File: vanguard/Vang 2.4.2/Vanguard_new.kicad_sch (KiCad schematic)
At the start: 84 parts, among them J1 USB_C_Receptacle_USB2.0_16P, J2 Micro_SD_Card_Det1, J3 Conn_02x03_Odd_Even, J4 Conn_01x03, J5 Conn_01x03, J6 Conn_01x03, J7 Conn_01x02_Pin, Q1 BSS138, Q2 BSS138, Q3 BSS138, Q4 BSS138, U1 TXB0104D, U10 AP2112K-3.3, U3 ATSAMD11D14A-M, U4 BMP390L, U5 BD1020HFV-TR, U6 AT25DF641A-SH-T, U7 ATmega4809-A, U9 TPS61092, Y1 Crystal

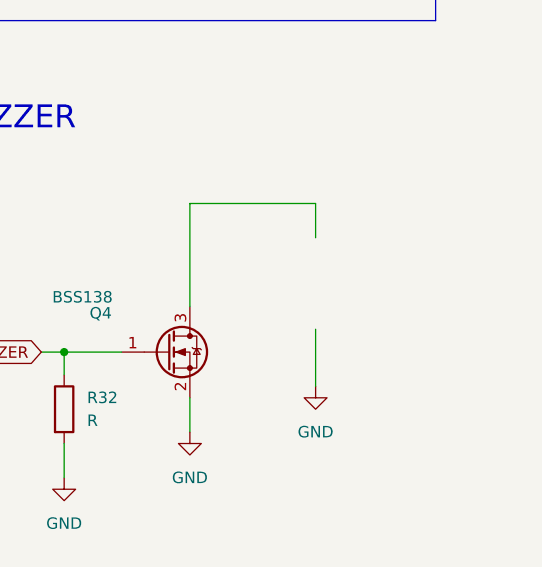
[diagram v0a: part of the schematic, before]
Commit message: added CMI-1295-0585T[1]
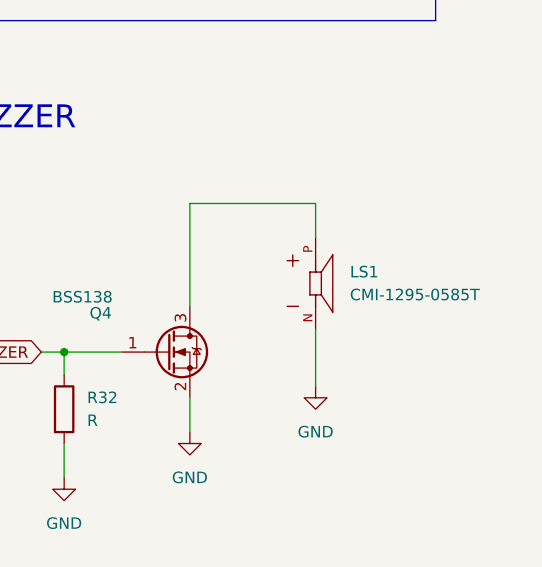
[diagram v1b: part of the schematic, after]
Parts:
- added LS1: CMI-1295-0585T, CMI-1295-0585T:CUI_CMI-1295-0585T, symbol CMI-1295-0585T[1]:CMI-1295-0585T
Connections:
- net GND: now also LS1.N
- net at Q4.3 (D): now also LS1.P
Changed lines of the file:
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@@
+	)
+	(symbol
+		(lib_id "CMI-1295-0585T[1]:CMI-1295-0585T")
+		(at 405.13 106.68 0)
+		(unit 1)
+		(exclude_from_sim no)
+		(in_bom yes)
+		(on_board yes)
+		(dnp no)
+		(fields_autoplaced yes)
+		(property "Reference" "LS1"
+			(at 408.94 105.4099 0)
+			(effects
+				(font
+					(size 1.27 1.27)
+				)
+				(justify left)
+			)
+		)
+		(property "Value" "CMI-1295-0585T"
+			(at 408.94 107.9499 0)
+			(effects
+				(font
+					(size 1.27 1.27)
+				)
+				(justify left)
+			)
+		)
+		(property "Footprint" "CMI-1295-0585T:CUI_CMI-1295-0585T"
+			(at 405.13 106.68 0)
+			(effects
+				(font
+					(size 1.27 1.27)
+				)
+				(justify bottom)
+				(hide yes)
+			)
+		)
+		(property "Datasheet" ""
+			(at 405.13 106.68 0)
+			(effects
+				(font
+					(size 1.27 1.27)
+				)
+				(hide yes)
+			)
+		)
+		(property "Description" ""
+			(at 405.13 106.68 0)
+			(effects
+				(font
+					(size 1.27 1.27)
+				)
+				(hide yes)
+			)
+		)
+		(property "MF" "Same Sky"
+			(at 405.13 106.68 0)
+			(effects
+				(font
+					(size 1.27 1.27)
+				)
+				(justify bottom)
+				(hide yes)
+			)
+		)
+		(property "MAXIMUM_PACKAGE_HEIGHT" "9.7mm"
+			(at 405.13 106.68 0)
+			(effects
+				(font
+					(size 1.27 1.27)
+				)
+				(justify bottom)
+				(hide yes)
+			)
+		)
+		(property "Package" "CUI Inc."
+			(at 405.13 106.68 0)
+			(effects
+				(font
+					(size 1.27 1.27)
+				)
+				(justify bottom)
+				(hide yes)
+			)
+		)
+		(property "Price" "None"
+			(at 405.13 106.68 0)
+			(effects
+				(font
+					(size 1.27 1.27)
+				)
+				(justify bottom)
+				(hide yes)
+			)
+		)
+		(property "Check_prices" "https://www.snapeda.com/parts/CMI-1295-0585T/Same+Sky/view-part/?ref=eda"
+			(at 405.13 106.68 0)
+			(effects
+				(font
+					(size 1.27 1.27)
+				)
+				(justify bottom)
+				(hide yes)
+			)
+		)
+		(property "STANDARD" "Manufacturer Recommendations"
+			(at 405.13 106.68 0)
+			(effects
+				(font
+					(size 1.27 1.27)
+				)
+				(justify bottom)
+				(hide yes)
+			)
+		)
+		(property "PARTREV" "N/A"
+			(at 405.13 106.68 0)
+			(effects
+				(font
+					(size 1.27 1.27)
+				)
+				(justify bottom)
+				(hide yes)
+			)
+		)
+		(property "SnapEDA_Link" "https://www.snapeda.com/parts/CMI-1295-0585T/Same+Sky/view-part/?ref=snap"
+			(at 405.13 106.68 0)
+			(effects
+				(font
+					(size 1.27 1.27)
+				)
+				(justify bottom)
+				(hide yes)
+			)
+		)
+		(property "MP" "CMI-1295-0585T"
+			(at 405.13 106.68 0)
+			(effects
+				(font
+					(size 1.27 1.27)
+				)
+				(justify bottom)
+				(hide yes)
+			)
+		)
+		(property "Description_1" "12 mm, 5 Vdc, 85 dB, Through Hole, Driving Circuit, Magnetic Audio Indicator Buzzer"
+			(at 405.13 106.68 0)
+			(effects
+				(font
+					(size 1.27 1.27)
+				)
+				(justify bottom)
+				(hide yes)
+			)
+		)
+		(property "Availability" "In Stock"
+			(at 405.13 106.68 0)
+			(effects
+				(font
+					(size 1.27 1.27)
+				)
+				(justify bottom)
+				(hide yes)
+			)
+		)
+		(property "MANUFACTURER" "CUI Inc"
+			(at 405.13 106.68 0)
+			(effects
+				(font
+					(size 1.27 1.27)
+				)
+				(justify bottom)
+				(hide yes)
+			)
+		)
+		(pin "N"
+		)
+		(pin "P"
+		)
+		(instances
+			(project ""
+				(path "/972fbf12-2dcd-4fdf-b1c9-8a2880c46640"
+					(reference "LS1")
+					(unit 1)
+				)
+			)
+		)
 	)
 	(symbol

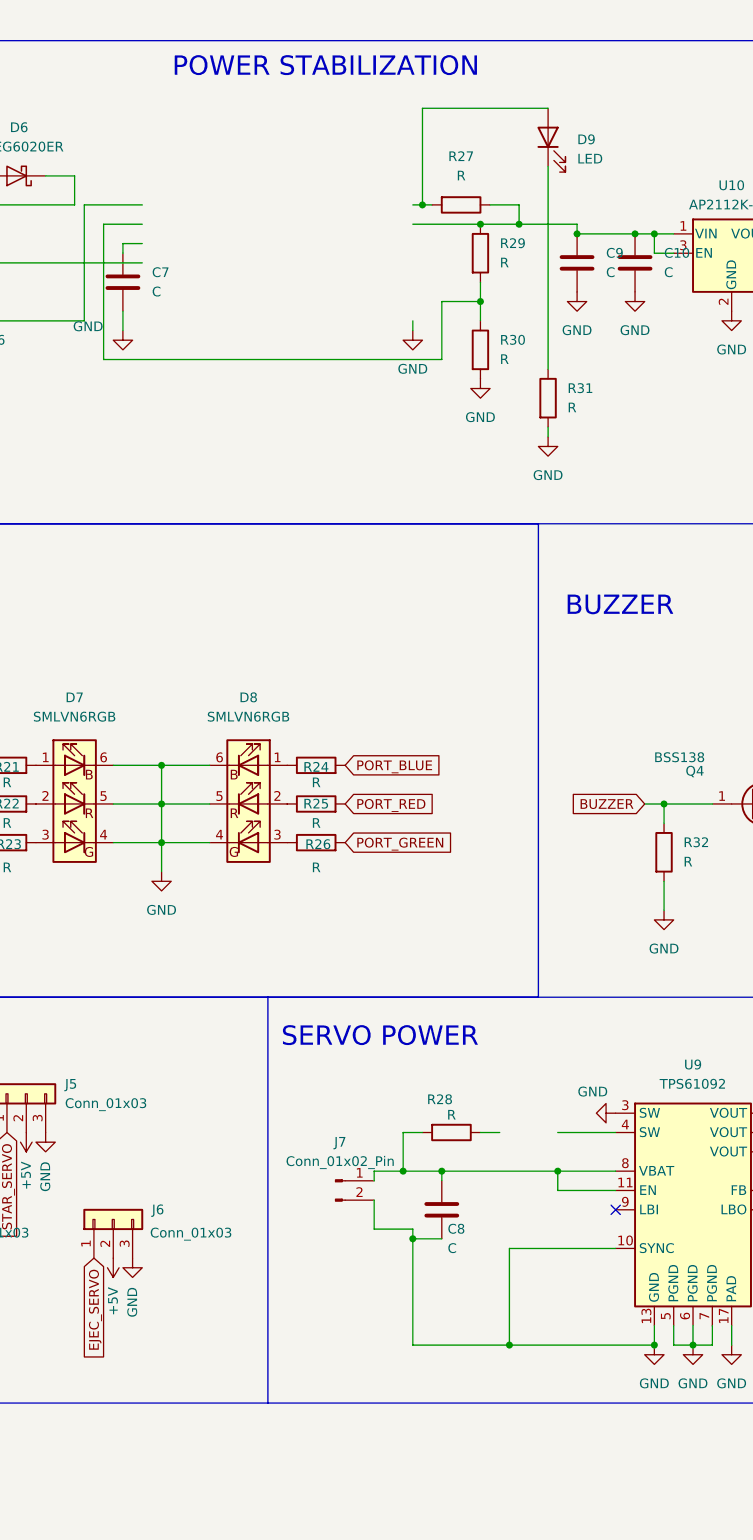
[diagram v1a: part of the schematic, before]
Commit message: added inductor and buck convertor
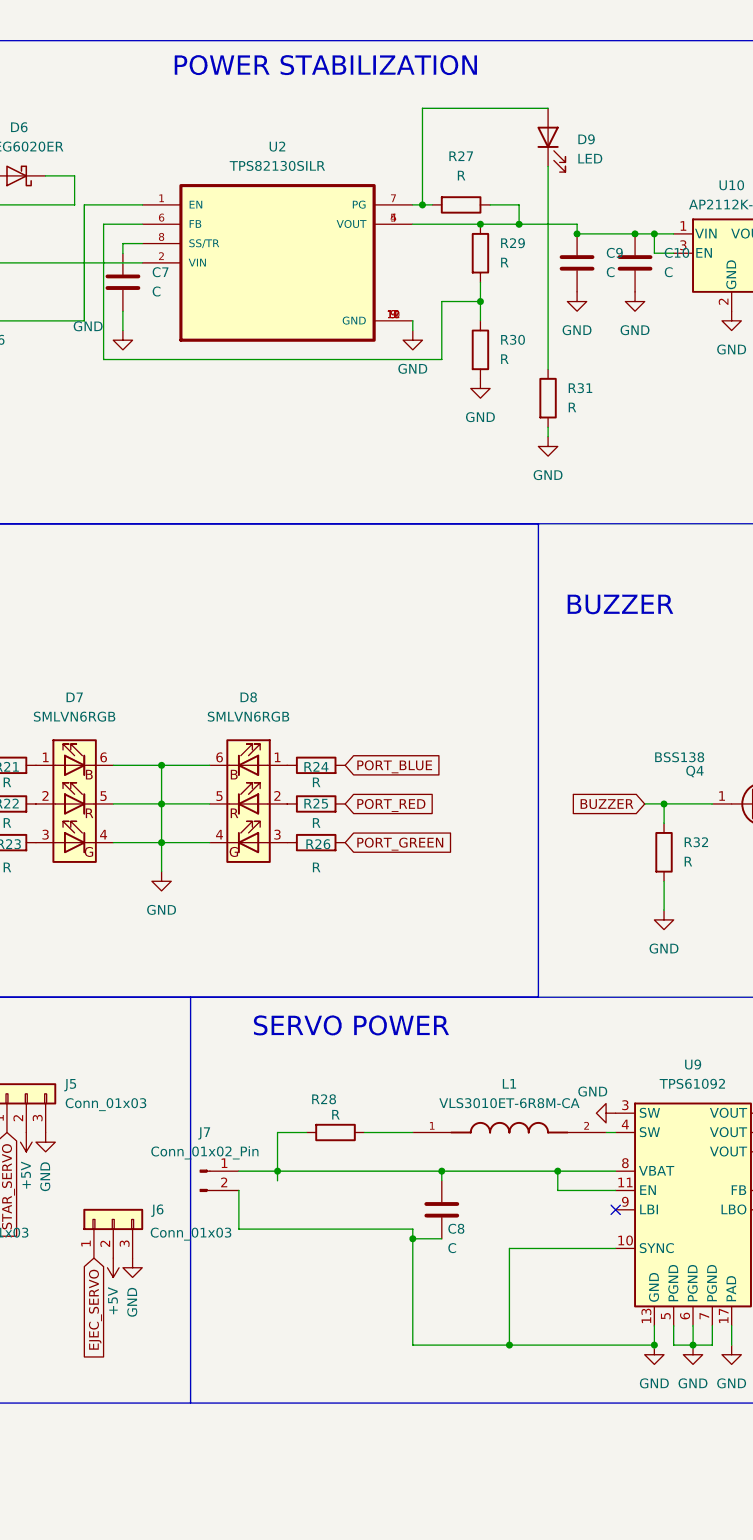
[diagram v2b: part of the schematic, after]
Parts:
- added L1: VLS3010ET-6R8M-CA, VLS3010ET-6R8M-CA:IND_VLS3010ET-6R8M-CA, symbol VLS3010ET-6R8M-CA[1]:VLS3010ET-6R8M-CA
- added U2: TPS82130SILR, TPS82130SILR:CONV_TPS82140SILR, symbol TPS82130SILR[1]:TPS82130SILR
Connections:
- net GND: now also U2.10 (GND), U2.11 (GND), U2.12 (GND), U2.3 (GND), U2.9 (GND)
- net at C10.1, C9.1, R27.1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: now also U2.4 (VOUT), U2.5 (VOUT)
- net at D9.2 (A), R27.2: now also U2.7 (PG)
- net at R29.2, R30.1: now also U2.6 (FB)
- net at C7.1: now also U2.8 (SS/TR)
- net at U9.4 (SW): now also L1.2
- net at R28.1: now also L1.1
- net at C6.1, D6.1 (K): now also U2.1 (EN), U2.2 (VIN)
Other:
- moved on the sheet: J7, R28

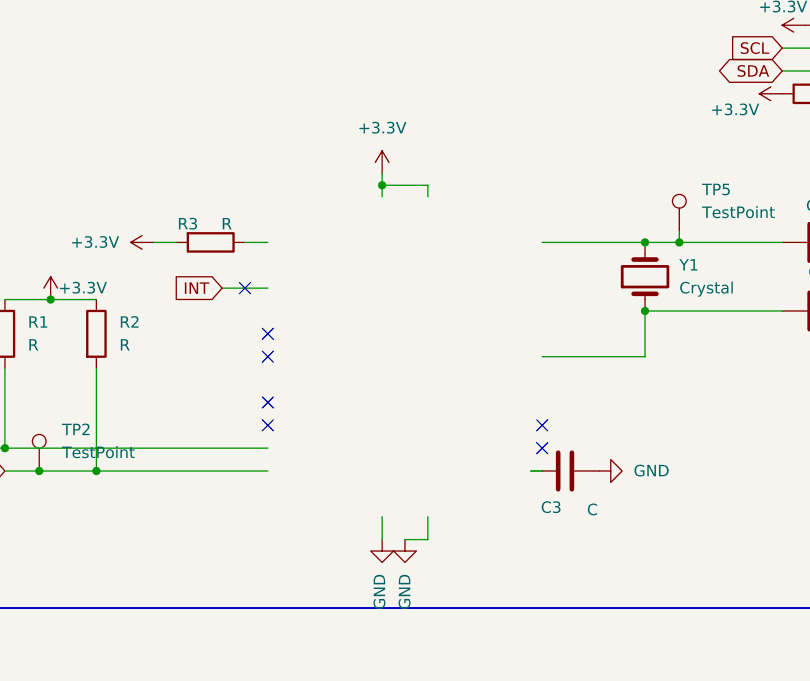
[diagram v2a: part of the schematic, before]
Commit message: BNO055 assigned
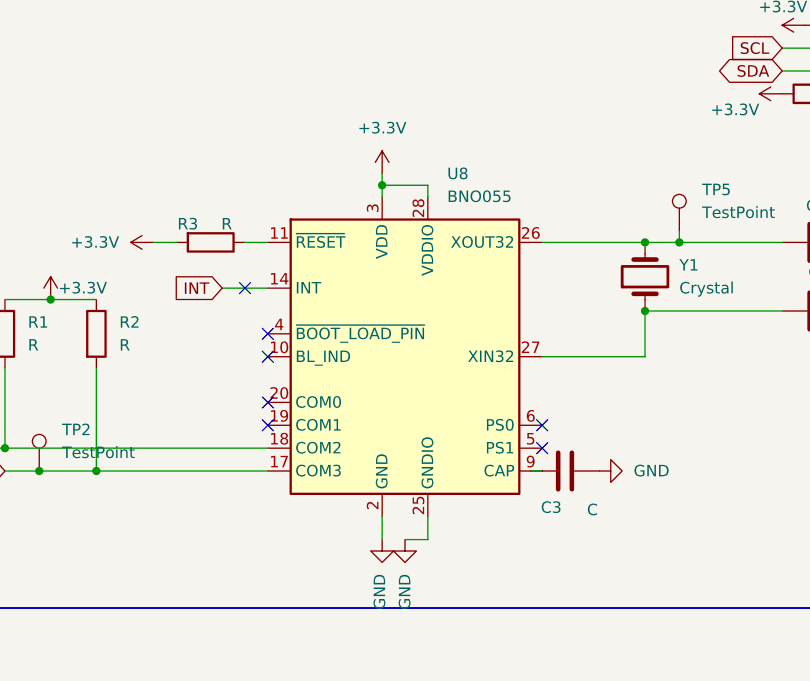
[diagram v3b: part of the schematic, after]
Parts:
- added U8: BNO055, Package_LGA:LGA-28_5.2x3.8mm_P0.5mm, symbol Sensor_Motion:BNO055
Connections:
- net +3.3V: now also U8.28 (VDDIO), U8.3 (VDD)
- net GND: now also U8.2 (GND), U8.25 (GNDIO)
- net INT: now also U8.14 (INT)
- net SCL: now also U8.17 (COM3)
- net SDA: now also U8.18 (COM2)
- net at C4.1, TP5.1, Y1.2: now also U8.26 (XOUT32)
- net at R3.1: now also U8.11 (~{RESET})
- net at C5.1, Y1.1: now also U8.27 (XIN32)
- net at C3.1: now also U8.9 (CAP)
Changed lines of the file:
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@@
+	)
+	(symbol
+		(lib_id "Sensor_Motion:BNO055")
+		(at 67.31 165.1 0)
+		(unit 1)
+		(exclude_from_sim no)
+		(in_bom yes)
+		(on_board yes)
+		(dnp no)
+		(fields_autoplaced yes)
+		(property "Reference" "U8"
+			(at 71.9933 144.78 0)
+			(effects
+				(font
+					(size 1.27 1.27)
+				)
+				(justify left)
+			)
+		)
+		(property "Value" "BNO055"
+			(at 71.9933 147.32 0)
+			(effects
+				(font
+					(size 1.27 1.27)
+				)
+				(justify left)
+			)
+		)
+		(property "Footprint" "Package_LGA:LGA-28_5.2x3.8mm_P0.5mm"
+			(at 73.66 181.61 0)
+			(effects
+				(font
+					(size 1.27 1.27)
+				)
+				(justify left)
+				(hide yes)
+			)
+		)
+		(property "Datasheet" "https://www.bosch-sensortec.com/media/boschsensortec/downloads/datasheets/bst-bno055-ds000.pdf"
+			(at 67.31 160.02 0)
+			(effects
+				(font
+					(size 1.27 1.27)
+				)
+				(hide yes)
+			)
+		)
+		(property "Description" "Intelligent 9-axis absolute orientation sensor, LGA-28"
+			(at 67.31 165.1 0)
+			(effects
+				(font
+					(size 1.27 1.27)
+				)
+				(hide yes)
+			)
+		)
+		(pin "24"
+		)
+		(pin "14"
+		)
+		(pin "22"
+		)
+		(pin "15"
+		)
+		(pin "4"
+		)
+		(pin "20"
+		)
+		(pin "7"
+		)
+		(pin "11"
+		)
+		(pin "17"
+		)
+		(pin "1"
+		)
+		(pin "3"
+		)
+		(pin "25"
+		)
+		(pin "23"
+		)
+		(pin "21"
+		)
+		(pin "6"
+		)
+		(pin "16"
+		)
+		(pin "2"
+		)
+		(pin "8"
+		)
+		(pin "12"
+		)
+		(pin "19"
+		)
+		(pin "27"
+		)
+		(pin "9"
+		)
+		(pin "13"
+		)
+		(pin "10"
+		)
+		(pin "5"
+		)
+		(pin "28"
+		)
+		(pin "18"
+		)
+		(pin "26"
+		)
+		(instances
+			(project ""
+				(path "/972fbf12-2dcd-4fdf-b1c9-8a2880c46640"
+					(reference "U8")
+					(unit 1)
+				)
+			)
+		)
 	)
 	(symbol

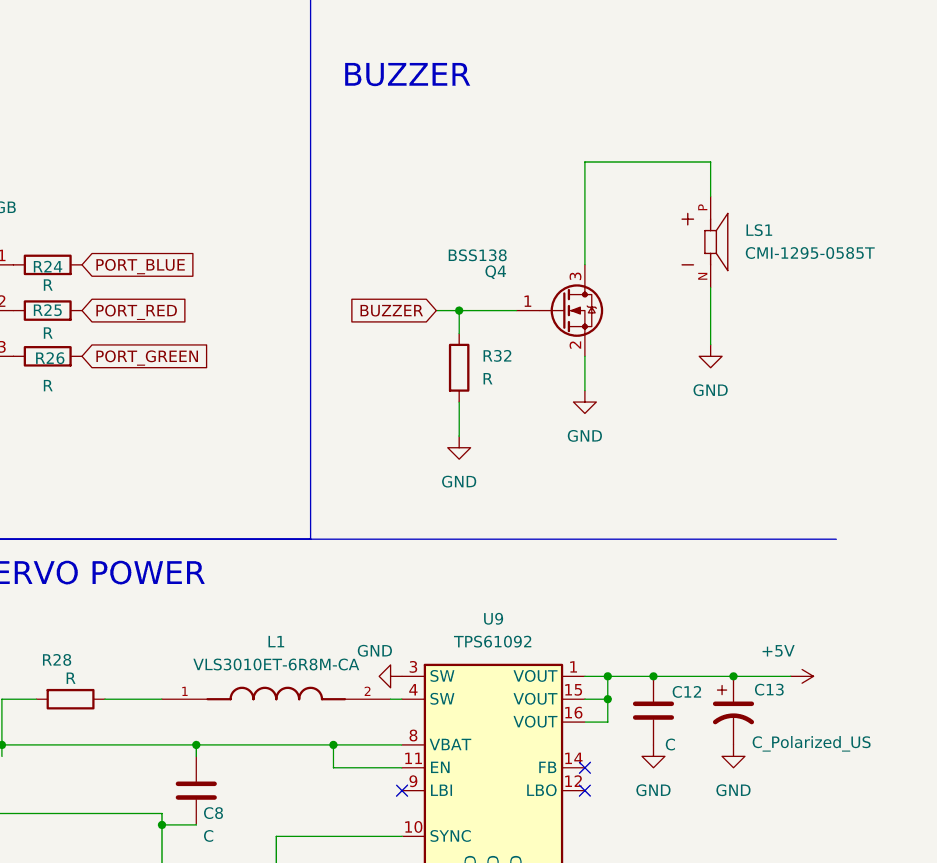
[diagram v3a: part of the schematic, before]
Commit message: changed buzzer circuit
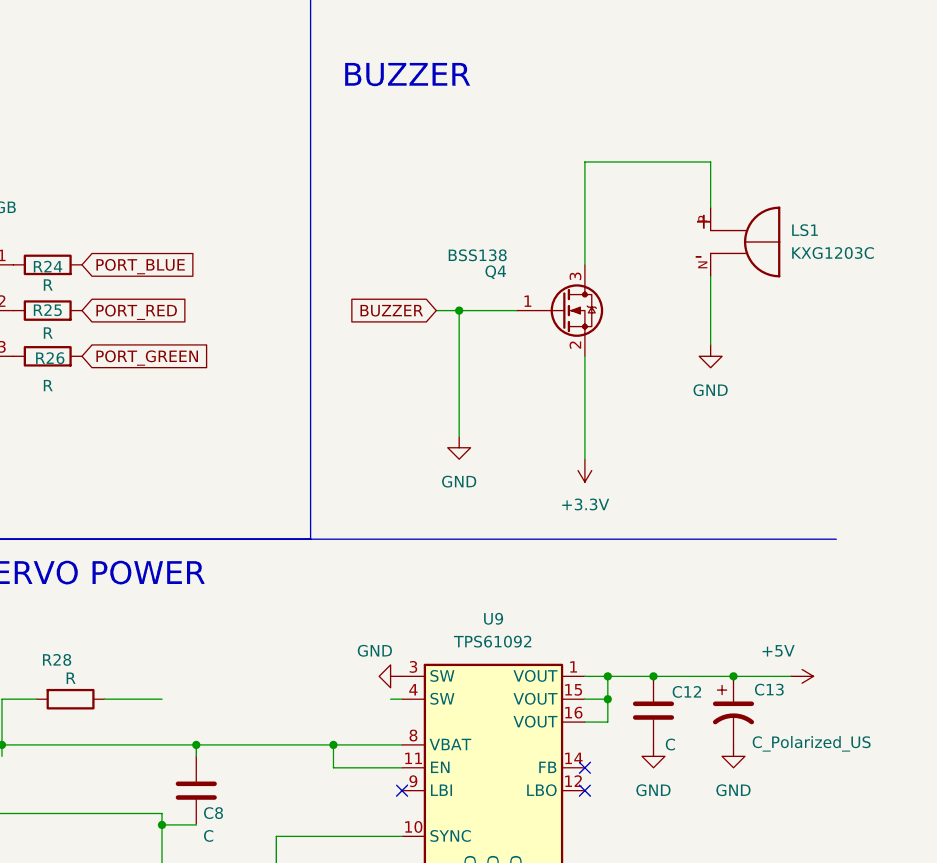
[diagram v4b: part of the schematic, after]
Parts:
- removed L1: VLS3010ET-6R8M-CA, VLS3010ET-6R8M-CA:IND_VLS3010ET-6R8M-CA, symbol VLS3010ET-6R8M-CA[1]:VLS3010ET-6R8M-CA
- removed LS1: CMI-1295-0585T, CMI-1295-0585T:CUI_CMI-1295-0585T, symbol CMI-1295-0585T[1]:CMI-1295-0585T
- removed R32: R, Resistor_SMD:R_0402_1005Metric, symbol Device:R
- added LS1: KXG1203C, KXG1203C:XDCR_KXG1203C, symbol KXG1203C[1]:KXG1203C
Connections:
- net BUZZER is gone; now on net GND: Q4.1 (G), U7.16 (PC4)
- net +3.3V: now also Q4.2 (S)
- net GND: now also LS1.N; no longer Q4.2 (S)
- net at Q4.3 (D): now also LS1.P
